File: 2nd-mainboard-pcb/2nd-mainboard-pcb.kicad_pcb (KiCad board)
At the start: 2 copper layers, 52 parts, among them J10 Servo Motor BL Touch, J11 T3, J12 Steckverbinder_Male_Fans, J15 Steckverbinder_Female_Motoren, J19 T2, J2 Fan_12/5V_Regelung, J20 T2, J21 T2, J22 T3, J3 FAN0, J4 FAN1, J5 FAN2, J6 FAN3, J7 Stepper Motor, J8 Servo Motor SM, J9 Microstepping, U12 MPU-6050, U7 TPM16050-S6TR, U8 RJK0456DPB-00-J5, U9 RJK0456DPB-00-J5

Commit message: fertiges layout platinen
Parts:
- added C1: 100nF, Capacitor_SMD:C_0402_1005Metric_Pad0.74x0.62mm_HandSolder, B.Cu at (176.9, 113.9)
- added C10: 100nF, Capacitor_SMD:C_0402_1005Metric_Pad0.74x0.62mm_HandSolder, B.Cu at (147.4, 118.4)
- added C11: 10µF, Capacitor_SMD:C_0805_2012Metric_Pad1.18x1.45mm_HandSolder, B.Cu at (147.7, 123.7)
- added C12: 10µF, Capacitor_SMD:C_0805_2012Metric_Pad1.18x1.45mm_HandSolder, B.Cu at (147.7, 125.9)
- added C13: 100nF, Capacitor_SMD:C_0402_1005Metric_Pad0.74x0.62mm_HandSolder, B.Cu at (148.4, 127.7)
- added C14: 22µF, Capacitor_SMD:C_1210_3225Metric_Pad1.33x2.70mm_HandSolder, B.Cu at (147.5, 107.4)
- added C15: 10µF, Capacitor_SMD:C_0805_2012Metric_Pad1.18x1.45mm_HandSolder, F.Cu at (147.5, 120.3)
- added C16: 100nF, Capacitor_SMD:C_0402_1005Metric_Pad0.74x0.62mm_HandSolder, B.Cu at (157.8, 133.4)
- added C17: 100nF, Capacitor_SMD:C_0402_1005Metric_Pad0.74x0.62mm_HandSolder, B.Cu at (157.8, 132.4)
- added C18: 1uF, Capacitor_SMD:C_0805_2012Metric_Pad1.18x1.45mm_HandSolder, B.Cu at (154.4, 133.2)
- added C19: 4.7uF, Capacitor_SMD:C_0805_2012Metric_Pad1.18x1.45mm_HandSolder, F.Cu at (151.9, 113.6)
- added C2: 22nF, Capacitor_SMD:C_1210_3225Metric_Pad1.33x2.70mm_HandSolder, F.Cu at (174.4, 107.3)
- added C20: 100nF, Capacitor_SMD:C_0402_1005Metric_Pad0.74x0.62mm_HandSolder, B.Cu at (151.2, 102.8)
- added C21: 18pF, Capacitor_SMD:C_0402_1005Metric_Pad0.74x0.62mm_HandSolder, B.Cu at (147.1, 112.8)
- added C22: 18pF, Capacitor_SMD:C_0402_1005Metric_Pad0.74x0.62mm_HandSolder, B.Cu at (147.1, 111.5)
- added C3: 10µF, Capacitor_SMD:C_0805_2012Metric_Pad1.18x1.45mm_HandSolder, B.Cu at (176.7, 122.1)
- added C4: 10µF, Capacitor_SMD:C_0805_2012Metric_Pad1.18x1.45mm_HandSolder, B.Cu at (175.6, 127.7)
- added C5: 10µF, Capacitor_SMD:C_1210_3225Metric_Pad1.33x2.70mm_HandSolder, B.Cu at (176.1, 124.9)
- added C6: 100nF, Capacitor_SMD:C_0402_1005Metric_Pad0.74x0.62mm_HandSolder, B.Cu at (178.2, 127.8)
- added C7: 100nF, Capacitor_SMD:C_0402_1005Metric_Pad0.74x0.62mm_HandSolder, B.Cu at (164.8, 128.1)
- added C8: 47µF, Capacitor_SMD:C_1210_3225Metric_Pad1.33x2.70mm_HandSolder, B.Cu at (176.1, 109.4)
- added C9: 22nF, Capacitor_SMD:C_1210_3225Metric_Pad1.33x2.70mm_HandSolder, F.Cu at (174.0, 110.6)
- added D1: WE-TVSP_DO-214AA_600W_BI, Imported_Component_Footprints:824521241, F.Cu at (156.1, 125.3)
- added D2: WE-TVSP_DO-214AA_600W_BI, Imported_Component_Footprints:824521241, F.Cu at (147.5, 125.5)
- added H5: MountHole, MountingHole:MountingHole_2.2mm_M2_Pad_TopBottom, F.Cu at (147.2, 102.9)
- added H6: MountHole, MountingHole:MountingHole_2.2mm_M2_Pad_TopBottom, F.Cu at (176.2, 102.9)
- added H7: MountHole, MountingHole:MountingHole_2.2mm_M2_Pad_TopBottom, F.Cu at (147.2, 131.9)
- added H8: MountHole, MountingHole:MountingHole_2.2mm_M2_Pad_TopBottom, F.Cu at (176.2, 131.9)
- added J1: PJ-082BH, Imported_Component_Footprints:CUI_PJ-082BH, F.Cu at (167.6, 133.6)
- added J13: Steckverbinder_Female_Leistung, Imported_Component_Footprints:SAMTEC_HLE-107-02-L-DV, B.Cu at (161.7, 105.4)
- added J14: Steckverbinder_Male_Leistung, Imported_Component_Footprints:SAMTEC_TSM-107-04-L-DV, F.Cu at (161.7, 105.4)
- added J16: ISP, Connector_PinHeader_2.54mm:PinHeader_2x03_P2.54mm_Vertical, F.Cu at (181.4, 133.2)
- added L1: 4.7µH, Imported_Component_Footprints:SPM10040T_4R7M_HZ, B.Cu at (167.7, 117.3)
- added L2: 3.3µH, Imported_Component_Footprints:IHLP2525CZER3R3M11, B.Cu at (152.4, 113.8)
- added P1: USB_C_Plug_USB2.0, Connector_USB:USB_C_Receptacle_GCT_USB4085, F.Cu at (152.7, 128.8)
- added R1: 100k, Resistor_SMD:R_0402_1005Metric, B.Cu at (164.9, 127.1)
- added R10: 5k1, Resistor_SMD:R_0402_1005Metric, B.Cu at (149.7, 129.1)
- added R11: 10k, Resistor_SMD:R_0402_1005Metric, F.Cu at (151.2, 121.6)
- added R2: 100k, Resistor_SMD:R_0402_1005Metric, B.Cu at (174.2, 120.0)
- added R3: 30k, Resistor_SMD:R_0402_1005Metric, F.Cu at (172.4, 104.9)
- added R4: 1k58, Resistor_SMD:R_0402_1005Metric, B.Cu at (175.3, 120.0)
- added R5: 30.1k, Resistor_SMD:R_0402_1005Metric, B.Cu at (176.4, 120.0)
- added R6: 10, Resistor_SMD:R_0402_1005Metric, B.Cu at (164.7, 129.1)
- added R7: 54.9k, Resistor_SMD:R_0402_1005Metric, B.Cu at (146.2, 115.7)
- added R8: 10k, Resistor_SMD:R_0402_1005Metric, B.Cu at (146.3, 116.8)
- added R9: 5k1, Resistor_SMD:R_0402_1005Metric, B.Cu at (156.6, 131.1)
- added U1: SQJ409EP-T1_GE3, Imported_Component_Footprints:SQJ409EP_T1_GE3, F.Cu at (175.5, 117.8)
- added U10: ATmega328PB-A, Package_QFP:TQFP-32_7x7mm_P0.8mm, F.Cu at (159.4, 116.8)
- added U2: SZ1SMB5927BT3G, Imported_Component_Footprints:SZ1SMB5927BT3G, F.Cu at (169.5, 117.3)
- added U3: TPS56837HRPAR, Imported_Component_Footprints:TPS56837HRPAR, B.Cu at (176.3, 116.6)
- added U4: TPS565208, Package_TO_SOT_SMD:SOT-23-6, B.Cu at (147.5, 120.8)
- added U5: FT232RL, Package_SO:SSOP-28_5.3x10.2mm_P0.65mm, B.Cu at (155.6, 123.1)
- added U6: PTS647SM38SMTR2LFS, Imported_Component_Footprints:SW_PTS647SM38SMTR2LFS_CNK, F.Cu at (176.2, 125.8)
- added Y1: ECS-160-18-4X-CKM, Imported_Component_Footprints:XTAL_ECS-160-18-4X-CKM, F.Cu at (147.6, 112.2)
- moved C27 2.55 mm to (202.2, 119.8), turned to -90 degrees
- moved C34 2.15 mm to (209.9, 117.8)
- moved TH1 1.82 mm to (209.3, 116.2)
- moved R26 1.81 mm to (210.0, 114.6)
- moved C24 1.13 mm to (210.1, 113.5), turned to 0 degrees
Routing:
- net GND: track 250.1 -> 572.3 mm, vias 10 -> 26
- net AREF: track 163.8 -> 306.7 mm, vias 3 -> 9
- net +12V: track 71.8 -> 163.0 mm, vias 2 -> 4
- net MOSI: track 35.9 -> 122.5 mm, vias 1 -> 3
- net +5V_USBC: track 0.00 -> 81.4 mm, vias 0 -> 7
- net RESET: track 3.71 -> 80.9 mm, vias 0 -> 5
- net PWR_IN_PROT: track 0.00 -> 37.7 mm, vias 0 -> 1
- net STEP: track 17.8 -> 52.1 mm, vias 0 -> 2
- net SCK: track 0.00 -> 32.6 mm, vias 0 -> 2
- net MISO: track 0.00 -> 28.9 mm, vias 0 -> 2
- net FAN_3_PWM: track 13.9 -> 39.0 mm, vias 0 -> 1
- net Net-(U3-SW): track 0.00 -> 25.0 mm, vias 0 -> 2
- net FAN_2_PWM: track 20.7 -> 44.4 mm, vias 0 -> 1
- net RXD: track 0.00 -> 22.9 mm, vias 0 -> 1
- net TXD: track 0.00 -> 22.6 mm, vias 0 -> 1
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- removed copper zone on B.Cu, net (none)
- removed copper zone on F.Cu, net (none)

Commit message: Testpoints hinzugefügt
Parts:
- added D7: GREEN, LED_SMD:LED_0805_2012Metric, F.Cu at (116.7, 108.4)
- added J18: Quartz, Connector_PinSocket_2.54mm:PinSocket_1x02_P2.54mm_Vertical, F.Cu at (97.1, 109.0)
- added J23: Conn_01x04_Socket, Connector_PinSocket_2.54mm:PinSocket_1x04_P2.54mm_Vertical, F.Cu at (120.4, 94.7)
- added R16: 1k, Resistor_SMD:R_0402_1005Metric, F.Cu at (113.9, 108.5)
- added R17: 10k, Resistor_SMD:R_0402_1005Metric, F.Cu at (137.6, 139.2)
- added TP18: ADC2, TestPoint:TestPoint_Pad_D2.0mm, F.Cu at (73.5, 63.7)
- added TP19: ADC3, TestPoint:TestPoint_Pad_D2.0mm, F.Cu at (69.5, 63.7)
- added TP2: GND_Test, TestPoint:TestPoint_Pad_D3.0mm, F.Cu at (126.9, 102.7)
- added TP20: ADC1, TestPoint:TestPoint_Pad_D2.0mm, F.Cu at (65.4, 63.7)
- added TP21: ADC0, TestPoint:TestPoint_Pad_D2.0mm, F.Cu at (61.4, 63.7)
- added TP22: I_Sense_5V, TestPoint:TestPoint_2Pads_Pitch2.54mm_Drill0.8mm, F.Cu at (121.0, 89.5)
- added TP23: I_Sense_5V, TestPoint:TestPoint_2Pads_Pitch2.54mm_Drill0.8mm, F.Cu at (124.3, 89.5)
- added TP25: I_Sense_12V, TestPoint:TestPoint_2Pads_Pitch2.54mm_Drill0.8mm, F.Cu at (127.7, 89.5)
- added TP3: 12V_Test, TestPoint:TestPoint_Pad_D3.0mm, F.Cu at (131.9, 102.7)
- added TP6: 5V_USBC_Test, TestPoint:TestPoint_Pad_D3.0mm, F.Cu at (116.9, 102.7)
- added TP7: 5V_POW_Test, TestPoint:TestPoint_Pad_D3.0mm, F.Cu at (121.9, 102.7)
- added TP8: Quartz_1, TestPoint:TestPoint_Loop_D3.80mm_Drill2.5mm, F.Cu at (96.6, 123.2)
- added TP9: Quartz_2, TestPoint:TestPoint_Loop_D3.80mm_Drill2.5mm, F.Cu at (96.6, 117.2)
- moved J9 143.4 mm to (82.7, 135.6)
- moved TH1 143.4 mm to (66.4, 127.2)
- moved A1 143.4 mm to (59.2, 134.9)
- moved C23 143.4 mm to (75.3, 132.5)
- moved C24 143.4 mm to (67.2, 124.5)
- moved C25 143.4 mm to (78.3, 142.0)
- moved C26 143.4 mm to (78.4, 143.8)
- moved C28 143.4 mm to (66.8, 142.0)
- moved C29 143.4 mm to (66.8, 143.8)
- moved C34 143.4 mm to (67.0, 128.8)
- moved H10 143.4 mm to (89.1, 114.0)
- moved H11 143.4 mm to (60.1, 143.0)
- moved H12 143.4 mm to (89.1, 143.0)
- moved H9 143.4 mm to (60.1, 114.0)
- moved J10 143.4 mm to (65.6, 139.5)
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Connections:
- A1 pad 13: AREF -> +5V_POW
- A1 pad 14: AREF -> +5V_POW
- C24 pad 1: AREF -> +5V_POW
- C25 pad 1: AREF -> +5V_POW
- C26 pad 1: AREF -> +5V_POW
- C27 pad 1: AREF -> +5V_POW
- C28 pad 1: AREF -> +5V_POW
- C29 pad 1: AREF -> +5V_POW
- J10 pad 2: AREF -> +5V_POW
- J12 pad 05: AREF -> +5V_POW
- J12 pad 07: +5V_USBC -> AREF
- J13 pad 02: +5V_USBC -> AREF
- J13 pad 05: AREF -> +5V_POW
- J14 pad 05: AREF -> +5V_POW
- J15 pad 05: AREF -> +5V_POW
- J16 pad 2: AREF -> +5V_POW
- J2 pad 1: AREF -> +5V_POW
- J8 pad 2: AREF -> +5V_POW
- J9 pad 01: AREF -> +5V_POW
- J9 pad 03: AREF -> +5V_POW
- J9 pad 05: AREF -> +5V_POW
- U10 pad 18: AREF -> +5V_POW
- U10 pad 4: AREF -> +5V_POW
- U12 pad 13: AREF -> +5V_POW
- U12 pad 8: AREF -> +5V_POW
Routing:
- net +5V_POW: track 0.00 -> 197.4 mm, vias 0 -> 7
- net GND: track 572.3 -> 475.3 mm, vias 26 -> 27
- net ADC0: track 35.9 -> 70.7 mm, vias 2 -> 3
- net Quartz_1: track 11.4 -> 41.5 mm
- net +5V_USBC: track 81.4 -> 108.9 mm, vias 7 -> 8
- net AREF: track 306.7 -> 333.9 mm
- net +12V: track 163.0 -> 189.8 mm, vias 4 -> 5
- net ADC3: track 49.6 -> 73.3 mm, vias 4 -> 6
- net ADC1: track 47.8 -> 68.2 mm, vias 2 -> 4
- net Quartz_2: track 15.1 -> 33.4 mm
- net ADC2: track 47.2 -> 63.6 mm
- net RESET: track 80.9 -> 93.0 mm, vias 5 -> 6
- net Net-(D7-K): track 0.00 -> 2.90 mm
- net SCK: track 32.6 -> 34.3 mm
- net LED_2: track 61.0 -> 62.6 mm
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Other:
- board text added: "By"
- board text added: "Fans & Temperatursensoren - Modul"
- board text added: "Fiber Printer"
- board text added: "J19"
- board text added: "Jan, Elias, Nico"
- board text added: "Microcontroller & Leistungs - Modul"
- board text added: "Servo- & Schrittmotoren - Modul"

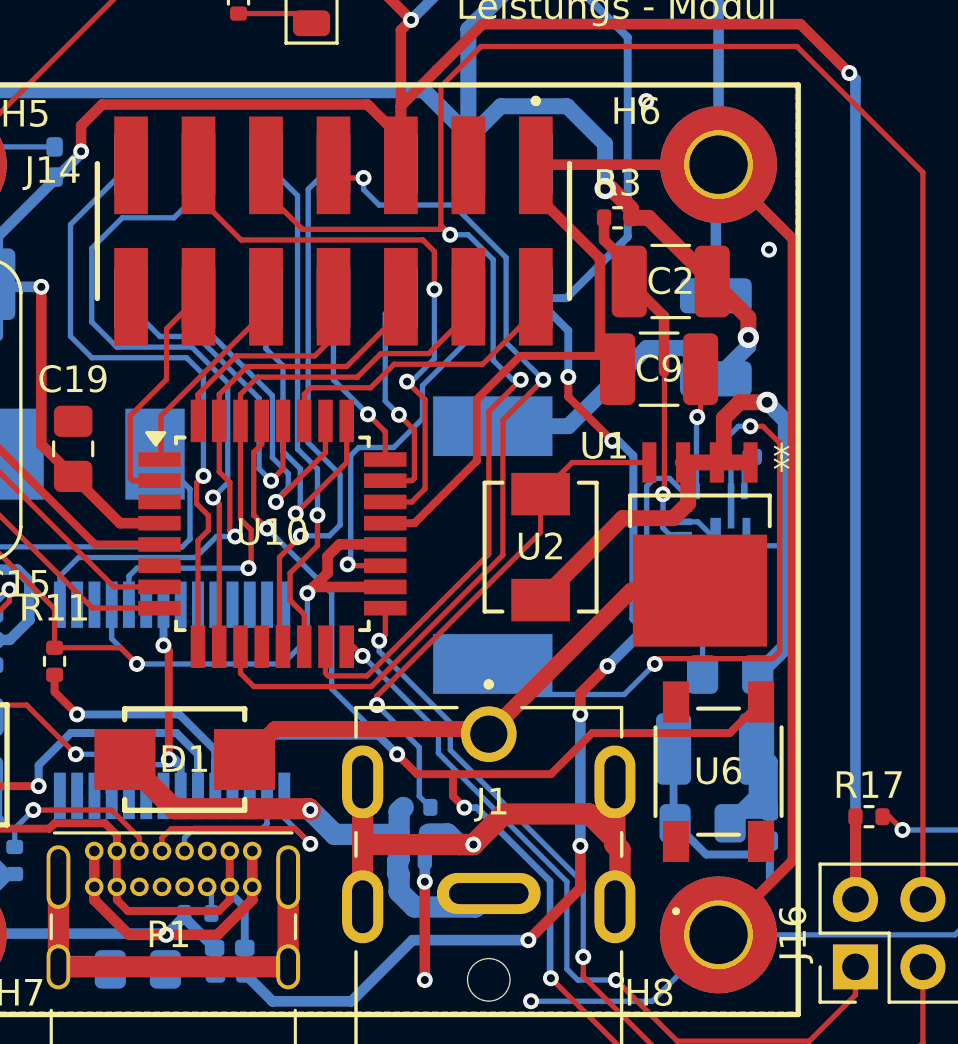
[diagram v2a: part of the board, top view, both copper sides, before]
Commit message: updated a bit of the track widths, removed comments in schematic
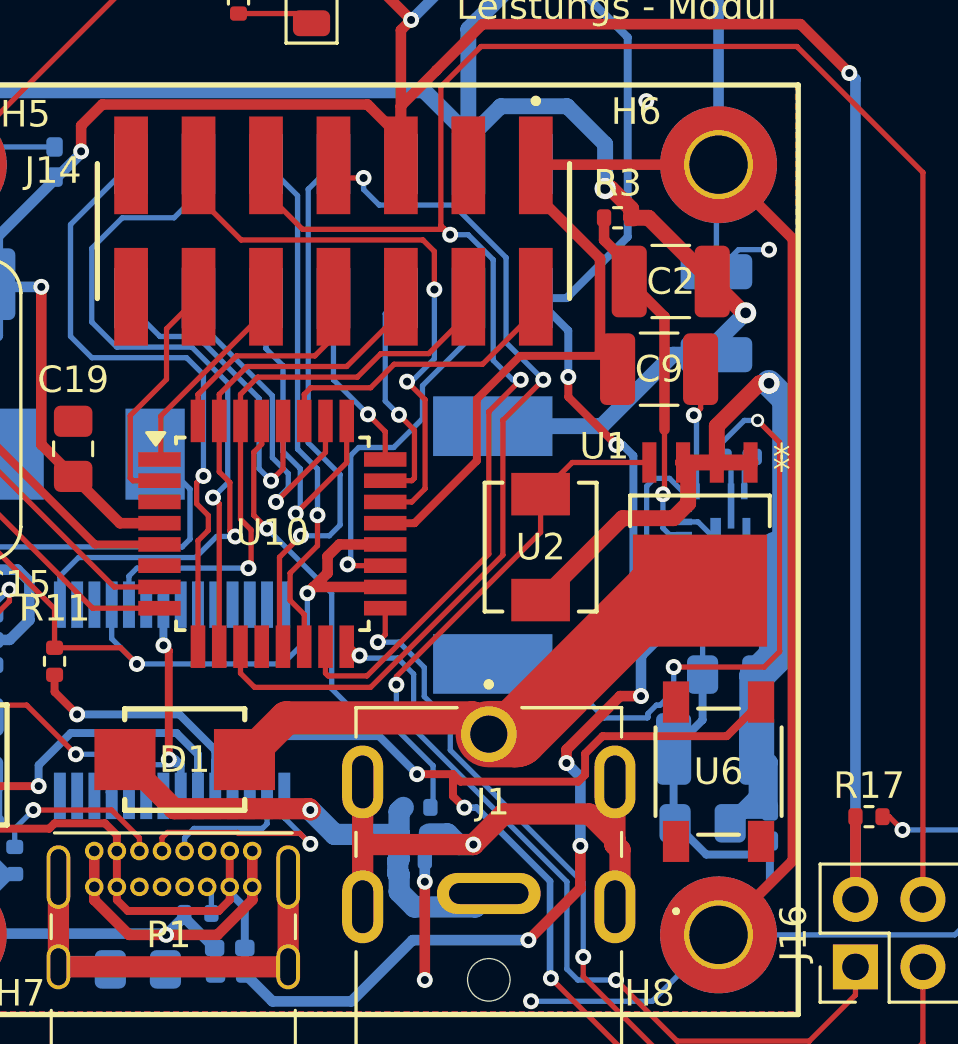
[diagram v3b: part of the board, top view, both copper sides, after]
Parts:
- moved C8 0.91 mm to (131.9, 120.3)
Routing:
- net RESET: track 93.0 -> 94.8 mm
- net Net-(U3-SW): track 25.0 -> 26.6 mm
- net +12V: track 189.8 -> 188.3 mm
- net GND: track 475.3 -> 476.8 mm
- net MISO: track 29.5 -> 30.2 mm
- net PWR_IN_PROT: track 37.7 -> 38.4 mm
- net Net-(U1-G): track 19.8 -> 19.2 mm
- net SCK: track 34.3 -> 34.8 mm

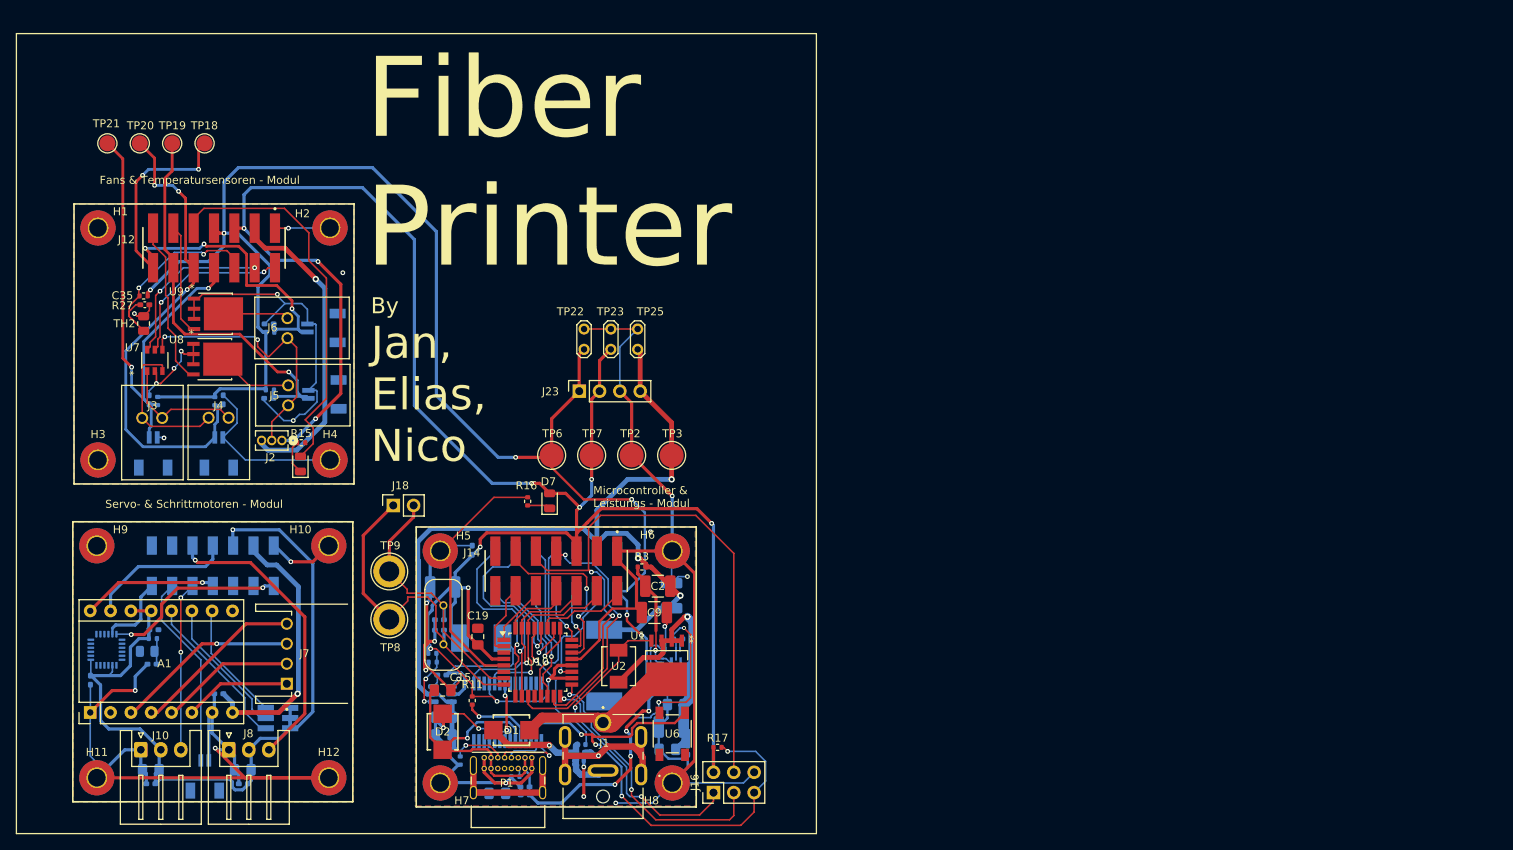
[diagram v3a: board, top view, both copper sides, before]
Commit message: kleine PCB Verbesserungen: edge.cuts fuer aussenkontur rund gemacht und cutout-funktion begonnen
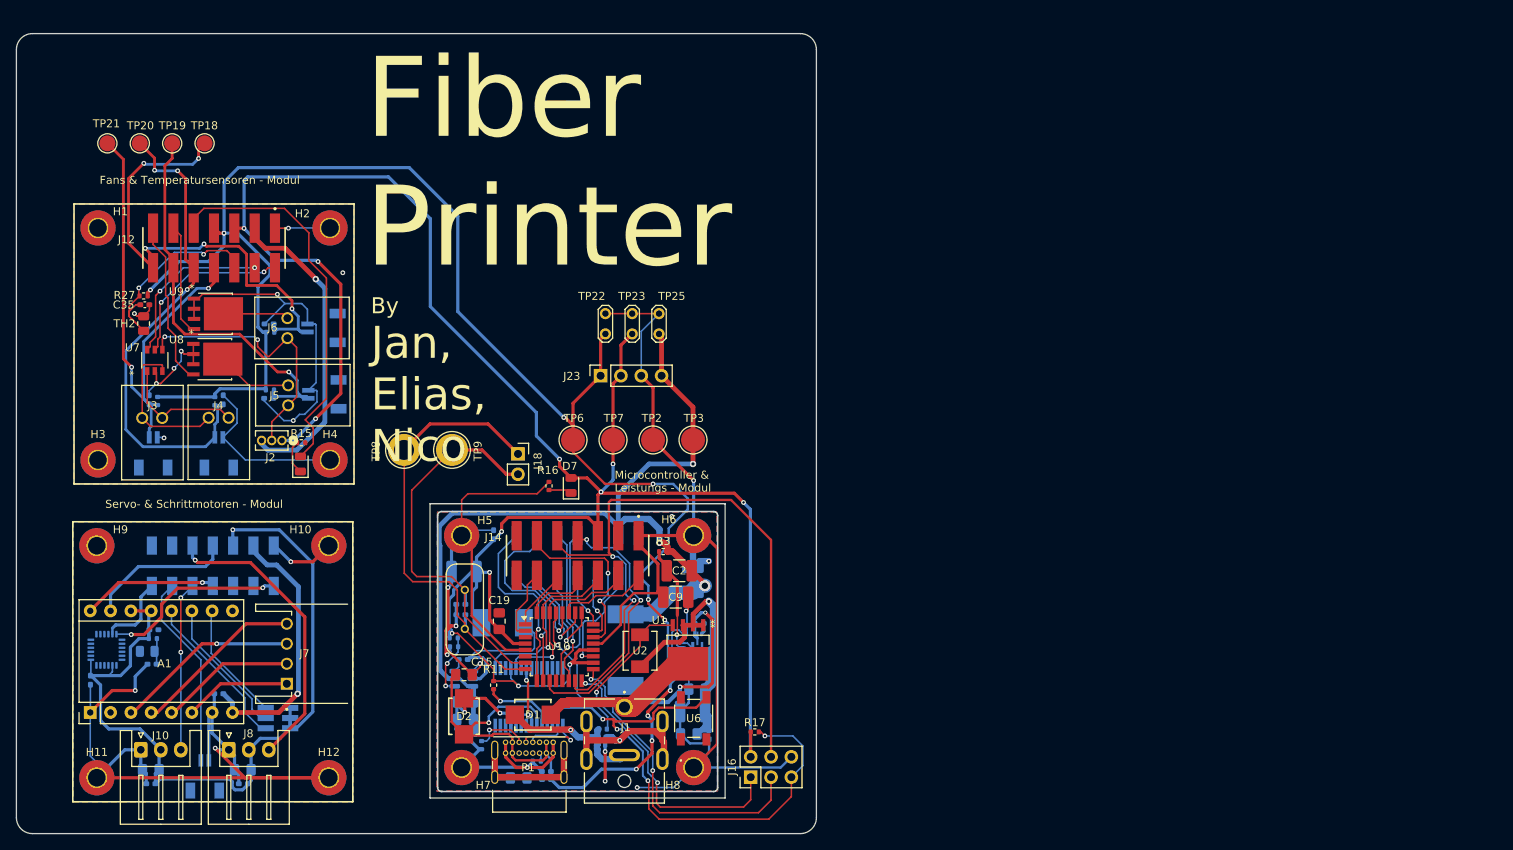
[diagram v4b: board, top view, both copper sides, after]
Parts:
- moved TP8 21.3 mm to (98.5, 102.0), turned to -90 degrees
- moved TP9 17.1 mm to (104.5, 102.0), turned to -90 degrees
- moved J18 16.9 mm to (112.7, 102.5), turned to 0 degrees
- moved J16 5.04 mm to (141.8, 142.9)
- moved R17 5.04 mm to (142.3, 137.3)
- moved C3 3.30 mm to (135.1, 131.9)
- moved C4 3.30 mm to (134.1, 137.5)
- moved U6 3.30 mm to (134.7, 135.6)
- moved H6 3.30 mm to (134.7, 112.7)
- moved C11 3.30 mm to (106.1, 133.5)
- moved C13 3.30 mm to (106.8, 137.5)
- moved C18 3.30 mm to (112.8, 143.0)
- moved C19 3.30 mm to (110.4, 123.4)
- moved C7 3.30 mm to (123.2, 137.9)
- moved D2 3.30 mm to (106.0, 135.3)
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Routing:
- net +5V_USBC: track 109.3 -> 81.3 mm, vias 8 -> 7
- net AREF: track 333.9 -> 360.0 mm, vias 9 -> 10
- net Quartz_2: track 33.4 -> 49.5 mm
- net Quartz_1: track 41.5 -> 56.8 mm
- net GND: track 476.8 -> 482.1 mm
- net MISO: track 30.2 -> 35.4 mm
- net SCK: track 34.8 -> 39.5 mm
- net RESET: track 94.8 -> 99.4 mm
- net MOSI: track 122.8 -> 125.6 mm
- net +12V: track 188.3 -> 189.4 mm
- net +5V_POW: track 197.4 -> 196.5 mm
- net ADC3: track 73.3 -> 74.1 mm
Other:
- board outline added: 100 x 100 mm

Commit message: etwas mit platinenumriss probiert
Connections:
- P1 pad A1: GND -> (no net)
- P1 pad A12: GND -> (no net)
- P1 pad A4: +5V_USBC -> (no net)
- P1 pad A5: Net-(P1-CC) -> (no net)
- P1 pad A6: USBD+ -> (no net)
- P1 pad A7: USBD- -> (no net)
- P1 pad A9: +5V_USBC -> (no net)
- P1 pad B1: GND -> (no net)
- P1 pad B12: GND -> (no net)
- P1 pad B4: +5V_USBC -> (no net)
- P1 pad B5: Net-(P1-VCONN) -> (no net)
- P1 pad B9: +5V_USBC -> (no net)
- P1 pad S1: Net-(P1-SHIELD) -> (no net)
- U5 pad 20: +5V_USBC -> AREF
- U5 pad 4: AREF -> +5V_POW
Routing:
- net GND: track 482.1 -> 477.9 mm
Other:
- board size 100 x 100 mm -> 36.9 x 36.8 mm
